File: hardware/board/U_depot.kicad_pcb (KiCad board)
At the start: 2 copper layers, 35.6 x 17.8 mm, 22 parts, among them P1 CAM, P2 TEENSY 3.2, P3 TEENSY 3.2, Q1 PBHV8118T,215, Q2 NTR5103NT1G, Q3 NTR5103NT1G, U1 LMC7101BYM5-TR

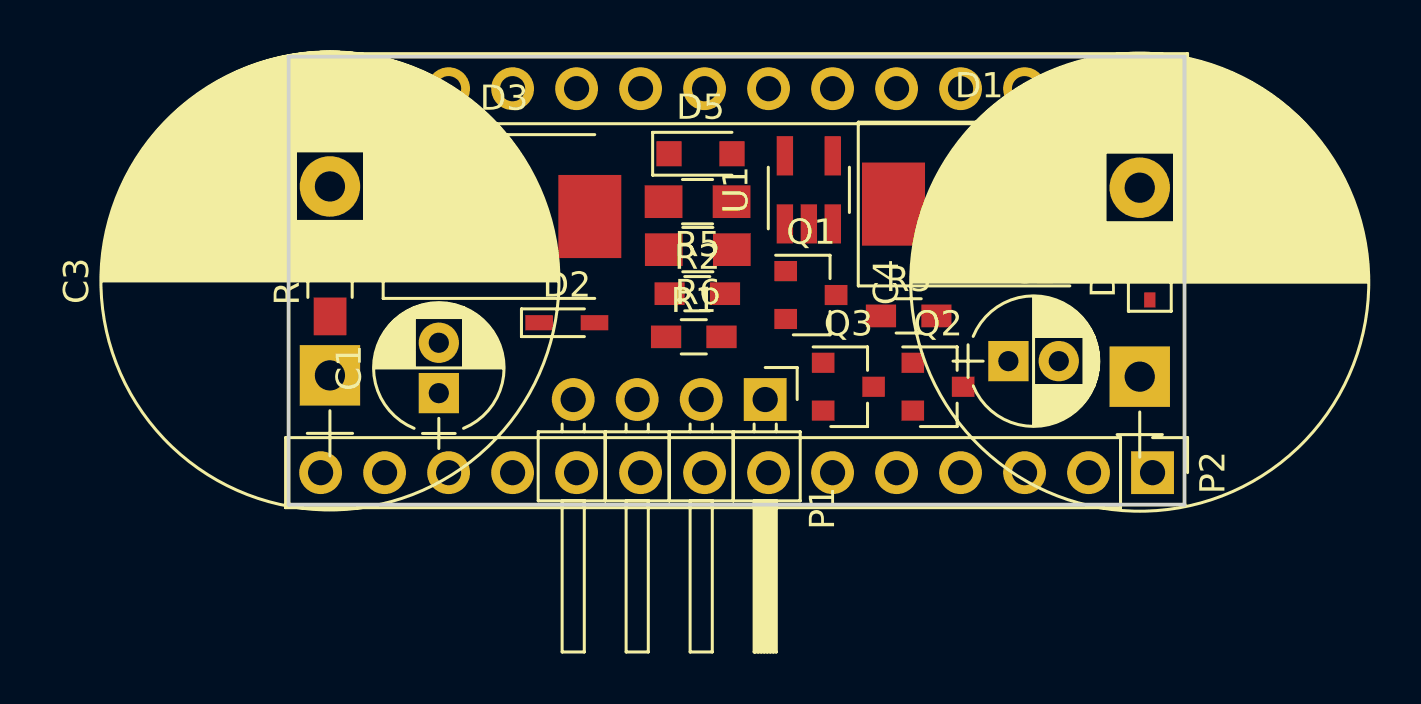
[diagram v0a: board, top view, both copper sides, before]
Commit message: updated schottky diode footprint
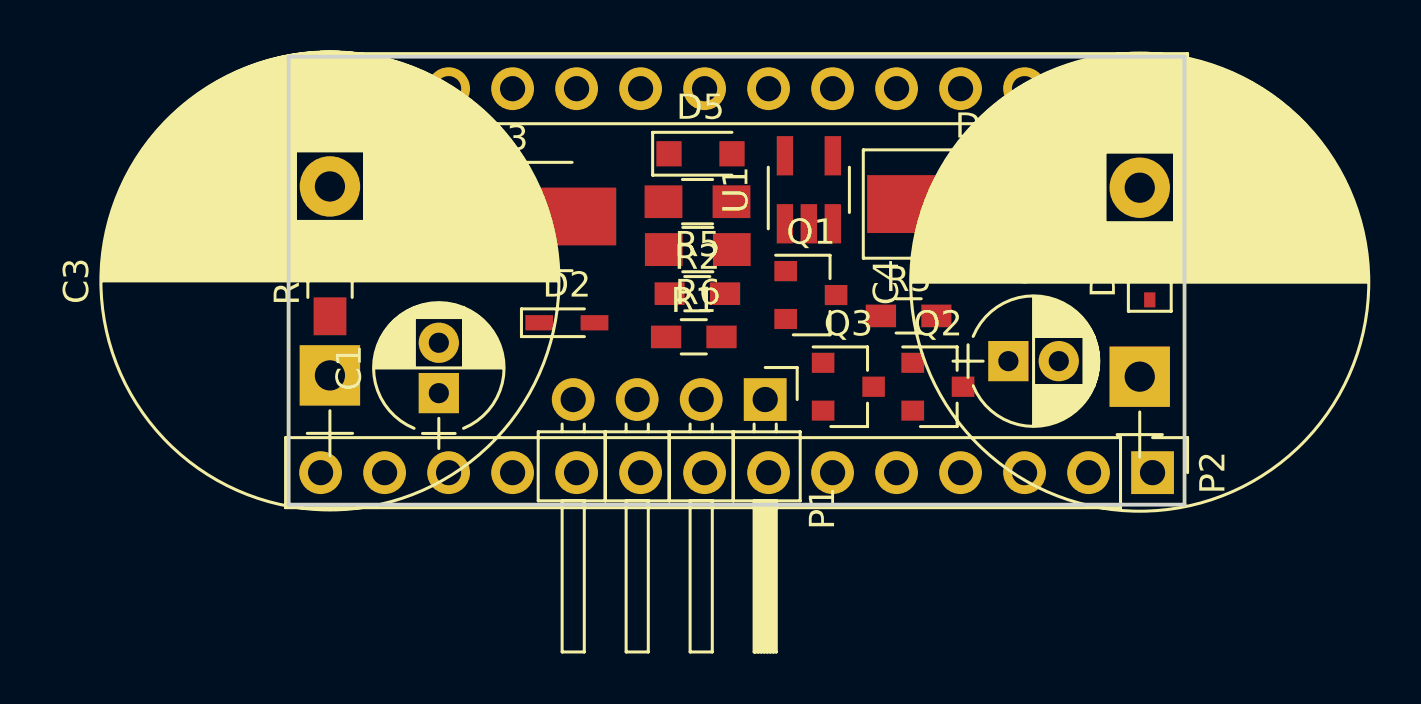
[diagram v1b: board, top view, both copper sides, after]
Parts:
- D1, D3: footprint Diodes_SMD:D_SMC_Standard -> Diodes_SMD:D_SMB_Handsoldering
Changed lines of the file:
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@@
     (links 33)
     (no_connects 33)
-    (area 178.874999 113.824999 214.585001 131.755001)
+    (area 86.553619 76.926419 122.263621 94.856421)
     (thickness 1.6)
     (drawings 4)
@@
     )
   )
-  (module Diodes_SMD:D_SMC_Standard (layer F.Cu)
-    (at 114.03838 82.84972)
-    (descr "Diode SMC Standard = DO-214AB")
-    (tags "Diode SMC Standard DO-214AB")
-    (attr smd)
-    (fp_text reference D1 (at 0 -4.7) (layer F.SilkS)
-      (effects (font (size 1 1) (thickness 0.15)))
-    )
-    (fp_text value LSM115JE3/TR13 (at 0 5.08) (layer F.Fab)
-      (effects (font (size 1 1) (thickness 0.15)))
-    )
-    (fp_line (start -4.8 3.25) (end -4.8 -3.25) (layer F.SilkS) (width 0.12))
-    (fp_line (start 3.55 3.1) (end -3.55 3.1) (layer F.Fab) (width 0.1))
-    (fp_line (start -3.55 3.1) (end -3.55 -3.1) (layer F.Fab) (width 0.1))
-    (fp_line (start 3.55 -3.1) (end 3.55 3.1) (layer F.Fab) (width 0.1))
-    (fp_line (start 3.55 -3.1) (end -3.55 -3.1) (layer F.Fab) (width 0.1))
-    (fp_line (start -4.9 -3.35) (end 4.9 -3.35) (layer F.CrtYd) (width 0.05))
-    (fp_line (start 4.9 -3.35) (end 4.9 3.35) (layer F.CrtYd) (width 0.05))
-    (fp_line (start 4.9 3.35) (end -4.9 3.35) (layer F.CrtYd) (width 0.05))
-    (fp_line (start -4.9 3.35) (end -4.9 -3.35) (layer F.CrtYd) (width 0.05))
-    (fp_line (start -0.64944 0.00102) (end -1.55114 0.00102) (layer F.Fab) (width 0.1))
-    (fp_line (start 0.50118 0.00102) (end 1.4994 0.00102) (layer F.Fab) (width 0.1))
-    (fp_line (start -0.64944 -0.79908) (end -0.64944 0.80112) (layer F.Fab) (width 0.1))
-    (fp_line (start 0.50118 0.75032) (end 0.50118 -0.79908) (layer F.Fab) (width 0.1))
-    (fp_line (start -0.64944 0.00102) (end 0.50118 0.75032) (layer F.Fab) (width 0.1))
-    (fp_line (start -0.64944 0.00102) (end 0.50118 -0.79908) (layer F.Fab) (width 0.1))
-    (fp_line (start -4.8 3.25) (end 3.6 3.25) (layer F.SilkS) (width 0.12))
-    (fp_line (start -4.8 -3.25) (end 3.6 -3.25) (layer F.SilkS) (width 0.12))
-    (pad 1 smd rect (at -3.4 0 90) (size 3.3 2.5) (layers F.Cu F.Paste F.Mask)
-      (net 7 "Net-(D1-Pad1)"))
-    (pad 2 smd rect (at 3.4 0 90) (size 3.3 2.5) (layers F.Cu F.Paste F.Mask)
-      (net 8 "Net-(D1-Pad2)"))
-    (model Diodes_SMD.3dshapes/D_SMC_Standard.wrl
-      (at (xyz 0 0 0))
-      (scale (xyz 0.3937 0.3937 0.3937))
-      (rotate (xyz 0 0 180))
-    )
-  )
   (module Diodes_SMD:D_SCD80_HandSoldering (layer F.Cu)
     (at 97.67062 87.56142)
@@
     (pad 1 smd rect (at -1.1 0) (size 1.1 0.6) (layers F.Cu F.Paste F.Mask)
       (net 9 "Net-(D2-Pad1)"))
-  )
-  (module Diodes_SMD:D_SMC_Standard (layer F.Cu)
-    (at 95.18142 83.34502)
-    (descr "Diode SMC Standard = DO-214AB")
-    (tags "Diode SMC Standard DO-214AB")
-    (attr smd)
-    (fp_text reference D3 (at 0 -4.7) (layer F.SilkS)
-      (effects (font (size 1 1) (thickness 0.15)))
-    )
-    (fp_text value LSM115JE3/TR13 (at 0 5.08) (layer F.Fab)
-      (effects (font (size 1 1) (thickness 0.15)))
-    )
-    (fp_line (start -4.8 3.25) (end -4.8 -3.25) (layer F.SilkS) (width 0.12))
-    (fp_line (start 3.55 3.1) (end -3.55 3.1) (layer F.Fab) (width 0.1))
-    (fp_line (start -3.55 3.1) (end -3.55 -3.1) (layer F.Fab) (width 0.1))
-    (fp_line (start 3.55 -3.1) (end 3.55 3.1) (layer F.Fab) (width 0.1))
-    (fp_line (start 3.55 -3.1) (end -3.55 -3.1) (layer F.Fab) (width 0.1))
-    (fp_line (start -4.9 -3.35) (end 4.9 -3.35) (layer F.CrtYd) (width 0.05))
-    (fp_line (start 4.9 -3.35) (end 4.9 3.35) (layer F.CrtYd) (width 0.05))
-    (fp_line (start 4.9 3.35) (end -4.9 3.35) (layer F.CrtYd) (width 0.05))
-    (fp_line (start -4.9 3.35) (end -4.9 -3.35) (layer F.CrtYd) (width 0.05))
-    (fp_line (start -0.64944 0.00102) (end -1.55114 0.00102) (layer F.Fab) (width 0.1))
-    (fp_line (start 0.50118 0.00102) (end 1.4994 0.00102) (layer F.Fab) (width 0.1))
-    (fp_line (start -0.64944 -0.79908) (end -0.64944 0.80112) (layer F.Fab) (width 0.1))
-    (fp_line (start 0.50118 0.75032) (end 0.50118 -0.79908) (layer F.Fab) (width 0.1))
-    (fp_line (start -0.64944 0.00102) (end 0.50118 0.75032) (layer F.Fab) (width 0.1))
-    (fp_line (start -0.64944 0.00102) (end 0.50118 -0.79908) (layer F.Fab) (width 0.1))
-    (fp_line (start -4.8 3.25) (end 3.6 3.25) (layer F.SilkS) (width 0.12))
-    (fp_line (start -4.8 -3.25) (end 3.6 -3.25) (layer F.SilkS) (width 0.12))
-    (pad 1 smd rect (at -3.4 0 90) (size 3.3 2.5) (layers F.Cu F.Paste F.Mask)
-      (net 7 "Net-(D1-Pad1)"))
-    (pad 2 smd rect (at 3.4 0 90) (size 3.3 2.5) (layers F.Cu F.Paste F.Mask)
-      (net 5 "Net-(C3-Pad1)"))
-    (model Diodes_SMD.3dshapes/D_SMC_Standard.wrl
-      (at (xyz 0 0 0))
-      (scale (xyz 0.3937 0.3937 0.3937))
-      (rotate (xyz 0 0 180))
-    )
   )
   (module Diodes_SMD:D_SOD-323 (layer F.Cu)
@@
     )
   )
+  (module Diodes_SMD:D_SMB_Handsoldering (layer F.Cu)
+    (at 114.03838 82.84972)
+    (descr "Diode SMB Handsoldering")
+    (tags "Diode SMB Handsoldering")
+    (attr smd)
+    (fp_text reference D1 (at 0 -3.1) (layer F.SilkS)
+      (effects (font (size 1 1) (thickness 0.15)))
+    )
+    (fp_text value LSM115JE3/TR13 (at 0.1 4.75) (layer F.Fab)
+      (effects (font (size 1 1) (thickness 0.15)))
+    )
+    (fp_line (start -4.6 -2.15) (end -4.6 2.15) (layer F.SilkS) (width 0.12))
+    (fp_line (start 2.3 2) (end -2.3 2) (layer F.Fab) (width 0.1))
+    (fp_line (start -2.3 2) (end -2.3 -2) (layer F.Fab) (width 0.1))
+    (fp_line (start 2.3 -2) (end 2.3 2) (layer F.Fab) (width 0.1))
+    (fp_line (start 2.3 -2) (end -2.3 -2) (layer F.Fab) (width 0.1))
+    (fp_line (start -4.7 -2.25) (end 4.7 -2.25) (layer F.CrtYd) (width 0.05))
+    (fp_line (start 4.7 -2.25) (end 4.7 2.25) (layer F.CrtYd) (width 0.05))
+    (fp_line (start 4.7 2.25) (end -4.7 2.25) (layer F.CrtYd) (width 0.05))
+    (fp_line (start -4.7 2.25) (end -4.7 -2.25) (layer F.CrtYd) (width 0.05))
+    (fp_line (start -0.64944 0.00102) (end -1.55114 0.00102) (layer F.Fab) (width 0.1))
+    (fp_line (start 0.50118 0.00102) (end 1.4994 0.00102) (layer F.Fab) (width 0.1))
+    (fp_line (start -0.64944 -0.79908) (end -0.64944 0.80112) (layer F.Fab) (width 0.1))
+    (fp_line (start 0.50118 0.75032) (end 0.50118 -0.79908) (layer F.Fab) (width 0.1))
+    (fp_line (start -0.64944 0.00102) (end 0.50118 0.75032) (layer F.Fab) (width 0.1))
+    (fp_line (start -0.64944 0.00102) (end 0.50118 -0.79908) (layer F.Fab) (width 0.1))
+    (fp_line (start -4.6 2.15) (end 2.7 2.15) (layer F.SilkS) (width 0.12))
+    (fp_line (start -4.6 -2.15) (end 2.7 -2.15) (layer F.SilkS) (width 0.12))
+    (pad 1 smd rect (at -2.7 0) (size 3.5 2.3) (layers F.Cu F.Paste F.Mask)
+      (net 7 "Net-(D1-Pad1)"))
+    (pad 2 smd rect (at 2.7 0) (size 3.5 2.3) (layers F.Cu F.Paste F.Mask)
+      (net 8 "Net-(D1-Pad2)"))
+    (model Diodes_SMD.3dshapes/D_SMB_Handsoldering.wrl
+      (at (xyz 0 0 0))
+      (scale (xyz 0.3937 0.3937 0.3937))
+      (rotate (xyz 0 0 180))
+    )
+  )
+  (module Diodes_SMD:D_SMB_Handsoldering (layer F.Cu)
+    (at 95.18142 83.34502)
+    (descr "Diode SMB Handsoldering")
+    (tags "Diode SMB Handsoldering")
+    (attr smd)
+    (fp_text reference D3 (at 0 -3.1) (layer F.SilkS)
+      (effects (font (size 1 1) (thickness 0.15)))
+    )
+    (fp_text value LSM115JE3/TR13 (at 0.1 4.75) (layer F.Fab)
+      (effects (font (size 1 1) (thickness 0.15)))
+    )
+    (fp_line (start -4.6 -2.15) (end -4.6 2.15) (layer F.SilkS) (width 0.12))
+    (fp_line (start 2.3 2) (end -2.3 2) (layer F.Fab) (width 0.1))
+    (fp_line (start -2.3 2) (end -2.3 -2) (layer F.Fab) (width 0.1))
+    (fp_line (start 2.3 -2) (end 2.3 2) (layer F.Fab) (width 0.1))
+    (fp_line (start 2.3 -2) (end -2.3 -2) (layer F.Fab) (width 0.1))
+    (fp_line (start -4.7 -2.25) (end 4.7 -2.25) (layer F.CrtYd) (width 0.05))
+    (fp_line (start 4.7 -2.25) (end 4.7 2.25) (layer F.CrtYd) (width 0.05))
+    (fp_line (start 4.7 2.25) (end -4.7 2.25) (layer F.CrtYd) (width 0.05))
+    (fp_line (start -4.7 2.25) (end -4.7 -2.25) (layer F.CrtYd) (width 0.05))
+    (fp_line (start -0.64944 0.00102) (end -1.55114 0.00102) (layer F.Fab) (width 0.1))
+    (fp_line (start 0.50118 0.00102) (end 1.4994 0.00102) (layer F.Fab) (width 0.1))
+    (fp_line (start -0.64944 -0.79908) (end -0.64944 0.80112) (layer F.Fab) (width 0.1))
+    (fp_line (start 0.50118 0.75032) (end 0.50118 -0.79908) (layer F.Fab) (width 0.1))
+    (fp_line (start -0.64944 0.00102) (end 0.50118 0.75032) (layer F.Fab) (width 0.1))
+    (fp_line (start -0.64944 0.00102) (end 0.50118 -0.79908) (layer F.Fab) (width 0.1))
+    (fp_line (start -4.6 2.15) (end 2.7 2.15) (layer F.SilkS) (width 0.12))
+    (fp_line (start -4.6 -2.15) (end 2.7 -2.15) (layer F.SilkS) (width 0.12))
+    (pad 1 smd rect (at -2.7 0) (size 3.5 2.3) (layers F.Cu F.Paste F.Mask)
+      (net 7 "Net-(D1-Pad1)"))
+    (pad 2 smd rect (at 2.7 0) (size 3.5 2.3) (layers F.Cu F.Paste F.Mask)
+      (net 5 "Net-(C3-Pad1)"))
+    (model Diodes_SMD.3dshapes/D_SMB_Handsoldering.wrl
+      (at (xyz 0 0 0))
+      (scale (xyz 0.3937 0.3937 0.3937))
+      (rotate (xyz 0 0 180))
+    )
+  )
